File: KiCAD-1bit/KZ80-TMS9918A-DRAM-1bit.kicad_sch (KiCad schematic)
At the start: 49 parts, among them J1 Conn_Coaxial, J2 EXT_JP, J3 SBC8080 BUS, J4 AD_JP, J5 AD_JP, Q1 2SC1815, U1 TMS9918A, U10 MB8118-16k-1bit-DRAM, U11 MB8118-16k-1bit-DRAM, U12 MB8118-16k-1bit-DRAM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

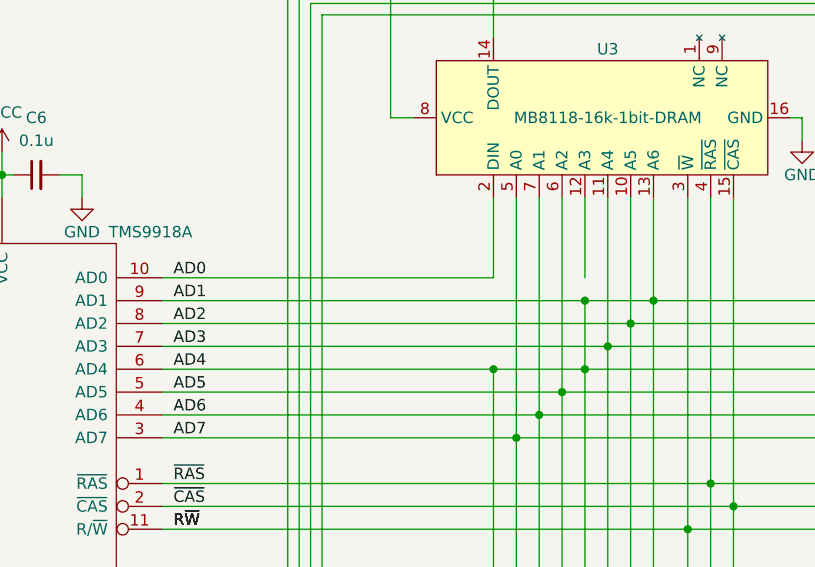
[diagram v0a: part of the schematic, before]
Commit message: 回路図バグ修正
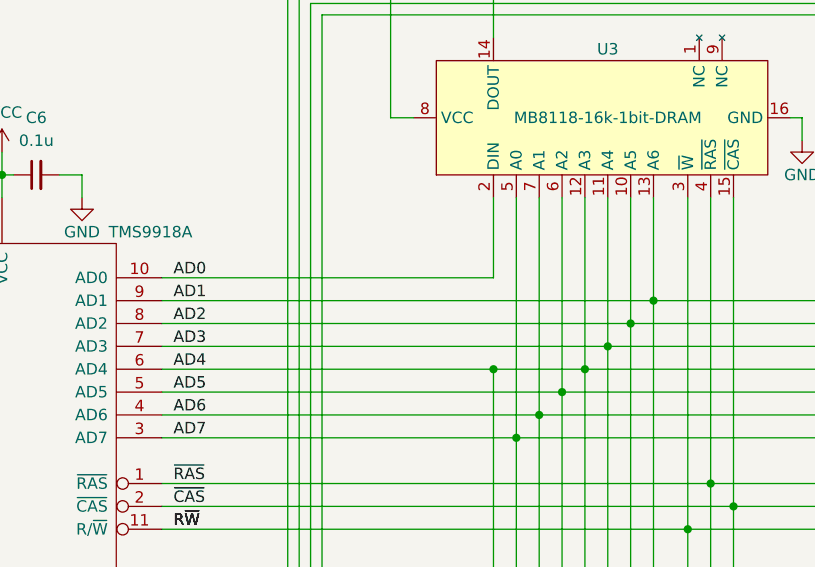
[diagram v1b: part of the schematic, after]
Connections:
- net AD1: no longer U1.6 (AD4), U10.12 (A3), U11.12 (A3), U12.12 (A3), U4.12 (A3), U7.12 (A3), U8.12 (A3), U9.12 (A3), U9.2 (DIN)
- net AD4: now reaches U3.12 (A3)
- net AD4: now also U1.6 (AD4), U10.12 (A3), U11.12 (A3), U12.12 (A3), U4.12 (A3), U7.12 (A3), U8.12 (A3), U9.12 (A3), U9.2 (DIN)
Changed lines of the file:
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@@
   (junction (at 129.54 86.36) (diameter 0) (color 0 0 0 0)
-  )
-  (junction (at 129.54 78.74) (diameter 0) (color 0 0 0 0)
   )
   (junction (at 107.95 39.37) (diameter 0) (color 0 0 0 0)
@@
     (stroke (width 0) (type default))
   )
-  (wire (pts (xy 129.54 67.31) (xy 129.54 76.2))
-    (stroke (width 0) (type default))
-  )
   (wire (pts (xy 267.97 93.98) (xy 267.97 140.97))
     (stroke (width 0) (type default))
@@
     (stroke (width 0) (type default))
   )
-  (wire (pts (xy 129.54 78.74) (xy 129.54 86.36))
+  (wire (pts (xy 129.54 67.31) (xy 129.54 86.36))
     (stroke (width 0) (type default))
   )
@@
     (stroke (width 0) (type default))
   )
-  (wire (pts (xy 82.55 78.74) (xy 129.54 78.74))
-    (stroke (width 0) (type default))
-  )
   (wire (pts (xy 26.67 95.25) (xy 26.67 97.79))
     (stroke (width 0) (type default))
@@
     (stroke (width 0) (type default))
   )
+  (wire (pts (xy 82.55 78.74) (xy 137.16 78.74))
+    (stroke (width 0) (type default))
+  )
   (wire (pts (xy 157.48 149.86) (xy 160.02 149.86))
     (stroke (width 0) (type default))
@@
     (stroke (width 0) (type default))
   )
-  (wire (pts (xy 129.54 78.74) (xy 137.16 78.74))
-    (stroke (width 0) (type default))
-  )

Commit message: DRAM 16kx1bit版プリントパターン作成
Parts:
- J1: footprint RCACon:RCAConAE -> RCA:RCAConAE

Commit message: 64k版 部品配置調整、16k版 4164 DRAM対応版 ガーバーデータ出力
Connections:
- net GND: now also U10.9 (NC), U11.9 (NC), U12.9 (NC), U3.9 (NC), U4.9 (NC), U7.9 (NC), U8.9 (NC), U9.9 (NC)
- no-connect marks 22 -> 30
